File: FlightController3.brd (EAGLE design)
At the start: 50 x 85 mm, 41 parts, among them U1 NUCLEO_L432KC

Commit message: Fixed several issues
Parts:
- moved LED_SCL 0.63 mm to (17.1, 5.08)
- renumbered LED_NAV_RX to NAV_RX, LED_NAV_TX to NAV_TX
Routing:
- net !SBUS: track 70.7 -> 55.0 mm, vias 2 -> 3
- net N$5: track 0.00 -> 1.66 mm
- net N$4: track 0.00 -> 1.66 mm
- net +5V: track 186.2 -> 185.8 mm, vias 3 -> 2
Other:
- board text added: "FlightControllerBoard v.1.0"

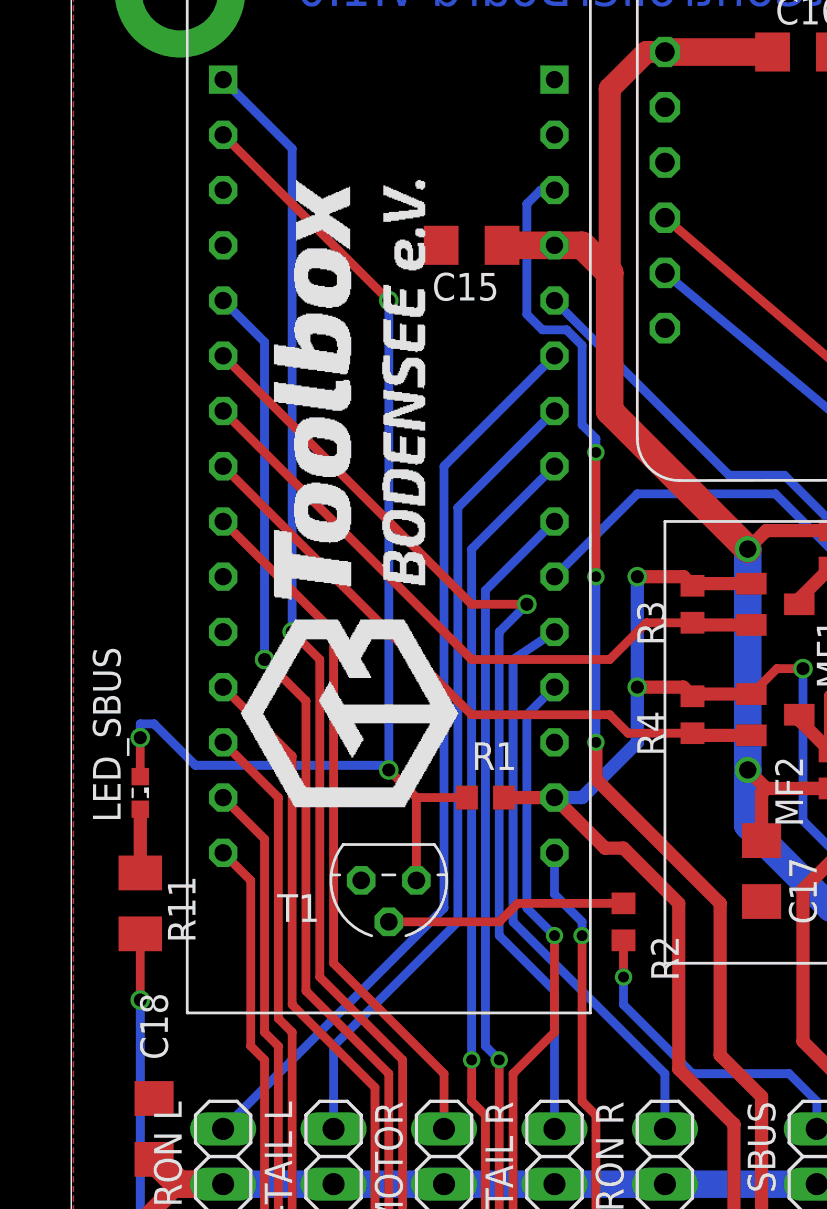
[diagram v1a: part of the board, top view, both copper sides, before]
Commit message: jumper to select between SBUS and !SBUS
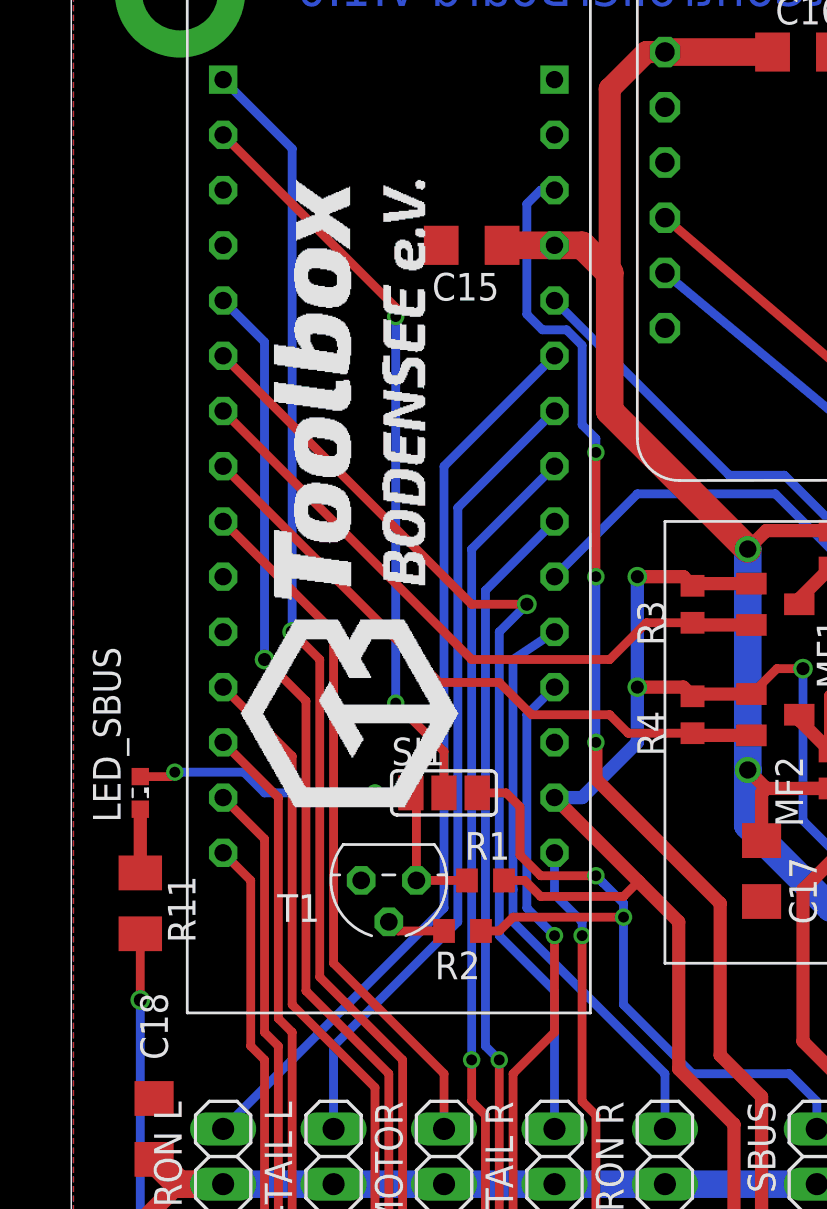
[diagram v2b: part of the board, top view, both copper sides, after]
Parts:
- added SJ1: (no value), jumper:SJ_2
- moved R2 7.42 mm to (18.0, 36.8), turned to 0 degrees
- moved R1 3.81 mm to (19.1, 39.2)
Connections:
- new net N$10: SJ1.2, U1.D0
- net !SBUS: now also SJ1.1; no longer U1.D0
- net SBUS: now also SJ1.3
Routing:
- net !SBUS: track 55.0 -> 19.4 mm, vias 3 -> 2
- net N$10: track 0.00 -> 34.5 mm, vias 0 -> 2
- net SBUS: track 15.0 -> 33.6 mm, vias 1 -> 2
- net N$1: track 11.1 -> 2.71 mm
- net +3V3: track 146.4 -> 150.4 mm

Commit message: eeprom and stuff
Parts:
- added U$3: AT24C16C, JonasLib:DIL08
- moved LED1 14.6 mm to (17.6, 3.81)
- moved R8 14.6 mm to (17.6, 7.62)
- moved LED2 14.6 mm to (21.2, 3.81)
- moved R7 14.6 mm to (21.2, 7.62)
- moved LED_SCL 4.62 mm to (12.7, 3.81)
- moved R12 4.49 mm to (10.8, 7.62)
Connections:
- net +5V: now also U$3.8
- net GND: now also U$3.4, U$3.7
- net SCL5V: now also U$3.6
- net SDA5V: now also U$3.5
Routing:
- net +5V: track 185.8 -> 177.8 mm
- net +3V3: track 150.4 -> 145.8 mm
- net SCL5V: track 116.8 -> 120.0 mm, vias 1 -> 2
- net SDA5V: track 105.1 -> 108.1 mm
- net !RST: track 87.6 -> 88.3 mm
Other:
- board text added: "P.L.A.N.E. v1.0"
- board text removed: "FlightControllerBoard v.1.0"

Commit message: various fixes
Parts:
- moved NAV_TX 0.63 mm to (42.5, 31.1)
- moved R9 0.63 mm to (42.5, 34.9)
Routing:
- net NAVBOARD_TX: track 50.1 -> 51.2 mm
- net +3V3: track 145.8 -> 145.2 mm
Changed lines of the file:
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@@
 <setting verticaltext="up"/>
 </settings>
-<grid distance="25" unitdist="mil" unit="mil" style="lines" multiple="1" display="yes" altdistance="0.025" altunitdist="inch" altunit="inch"/>
+<grid distance="25" unitdist="mil" unit="mm" style="lines" multiple="1" display="yes" altdistance="12.5" altunitdist="mil" altunit="mil"/>
 <layers>
 <layer number="1" name="Top" color="4" fill="1" visible="yes" active="yes"/>
@@
 <layer number="24" name="bOrigins" color="15" fill="1" visible="yes" active="yes"/>
 <layer number="25" name="tNames" color="7" fill="1" visible="yes" active="yes"/>
-<layer number="26" name="bNames" color="7" fill="1" visible="no" active="yes"/>
+<layer number="26" name="bNames" color="7" fill="1" visible="yes" active="yes"/>
 <layer number="27" name="tValues" color="7" fill="1" visible="no" active="yes"/>
 <layer number="28" name="bValues" color="7" fill="1" visible="no" active="yes"/>
@@
 </element>
 <element name="U$1" library="toolbox" package="TOOLBOX" value="TOOLBOX_LOGO" x="17.78" y="42.545" rot="R90"/>
-<element name="NAV_TX" library="led" library_urn="urn:adsk.eagle:library:259" package="SML0603" value="" x="43.18" y="31.115" smashed="yes" rot="R90">
-<attribute name="NAME" x="45.99" y="30.75" size="1.27" layer="25" rot="R90"/>
-<attribute name="VALUE" x="45.18" y="30.115" size="1.27" layer="27" rot="R90"/>
+<element name="NAV_TX" library="led" library_urn="urn:adsk.eagle:library:259" package="SML0603" value="" x="42.545" y="31.115" smashed="yes" rot="R90">
+<attribute name="NAME" x="45.355" y="30.75" size="1.27" layer="25" rot="R90"/>
+<attribute name="VALUE" x="44.545" y="30.115" size="1.27" layer="27" rot="R90"/>
 </element>
 <element name="NAV_RX" library="led" library_urn="urn:adsk.eagle:library:259" package="SML0603" value="" x="38.1" y="31.115" smashed="yes" rot="R90">
@@
 <attribute name="VALUE" x="40.1" y="30.115" size="1.27" layer="27" rot="R90"/>
 </element>
-<element name="R9" library="rcl" library_urn="urn:adsk.eagle:library:334" package="M1206" value="110" x="43.18" y="34.925" smashed="yes" rot="R90">
-<attribute name="NAME" x="41.91" y="33.655" size="1.27" layer="25" rot="R90"/>
-<attribute name="VALUE" x="45.72" y="33.655" size="1.27" layer="27" rot="R90"/>
+<element name="R9" library="rcl" library_urn="urn:adsk.eagle:library:334" package="M1206" value="110" x="42.545" y="34.925" smashed="yes" rot="R90">
+<attribute name="NAME" x="41.275" y="33.655" size="1.27" layer="25" rot="R90"/>
+<attribute name="VALUE" x="45.085" y="33.655" size="1.27" layer="27" rot="R90"/>
 </element>
 <element name="R10" library="rcl" library_urn="urn:adsk.eagle:library:334" package="M1206" value="110" x="38.1" y="34.925" smashed="yes" rot="R90">
@@
 <contactref element="U$3" pad="4"/>
 <contactref element="U$3" pad="7"/>
+<via x="11.43" y="30.48" extent="1-16" drill="0.35" shape="octagon"/>
+<via x="16.1925" y="29.5275" extent="1-16" drill="0.35" shape="octagon"/>
+<via x="22.5425" y="31.115" extent="1-16" drill="0.35" shape="octagon"/>
 </signal>
 <signal name="VIN">
@@
 <wire x1="22.225" y1="25.185" x2="27.305" y2="25.185" width="1.27" layer="16"/>
 <wire x1="45.085" y1="25.185" x2="46.355" y2="26.455" width="1.27" layer="16"/>
-<wire x1="46.355" y1="26.455" x2="46.355" y2="27.725" width="1.016" layer="16"/>
+<wire x1="46.355" y1="26.455" x2="46.355" y2="27.725" width="1.27" layer="16"/>
 <wire x1="23.495" y1="68.365" x2="22.225" y2="68.365" width="1.27" layer="1"/>
 <wire x1="24.765" y1="67.095" x2="23.495" y2="68.365" width="1.27" layer="1"/>
@@
 <wire x1="31.965" y1="55.245" x2="34.925" y2="55.245" width="0.6096" layer="1"/>
 <contactref element="C12" pad="1"/>
-<wire x1="46.355" y1="23.915" x2="46.355" y2="22.01" width="1.016" layer="16"/>
+<wire x1="46.355" y1="23.915" x2="46.355" y2="22.01" width="1.27" layer="16"/>
 <wire x1="46.355" y1="23.915" x2="45.085" y2="25.185" width="1.27" layer="16"/>
 <wire x1="31.965" y1="43.385" x2="31.115" y2="44.235" width="0.6096" layer="1"/>
@@
 <wire x1="4.95" y1="25.185" x2="6.985" y2="25.185" width="1.27" layer="1"/>
 <wire x1="4.95" y1="25.185" x2="3.81" y2="26.325" width="1.27" layer="1"/>
-<wire x1="2.54" y1="14.39" x2="4.445" y2="12.485" width="0.8128" layer="1"/>
-<wire x1="2.54" y1="22.775" x2="2.54" y2="14.39" width="0.8128" layer="1"/>
-<wire x1="2.54" y1="22.775" x2="4.95" y2="25.185" width="0.8128" layer="1"/>
+<wire x1="2.54" y1="14.39" x2="4.445" y2="12.485" width="1.27" layer="1"/>
+<wire x1="2.54" y1="22.775" x2="2.54" y2="14.39" width="1.27" layer="1"/>
+<wire x1="2.54" y1="22.775" x2="4.95" y2="25.185" width="1.27" layer="1"/>
 <wire x1="33.515" y1="43.385" x2="34.925" y2="43.385" width="0.6096" layer="1"/>
 <wire x1="35.14" y1="38.1" x2="34.925" y2="37.885" width="0.6096" layer="16"/>
-<wire x1="27.305" y1="77.255" x2="26.455" y2="77.255" width="1.016" layer="1"/>
-<wire x1="24.765" y1="75.565" x2="24.765" y2="67.095" width="1.016" layer="1"/>
-<wire x1="26.455" y1="77.255" x2="24.765" y2="75.565" width="1.016" layer="1"/>
+<wire x1="27.305" y1="77.255" x2="26.455" y2="77.255" width="1.27" layer="1"/>
+<wire x1="24.765" y1="75.565" x2="24.765" y2="67.095" width="1.27" layer="1"/>
+<wire x1="26.455" y1="77.255" x2="24.765" y2="75.565" width="1.27" layer="1"/>
 <contactref element="R12" pad="2"/>
 <wire x1="31.75" y1="40.985" x2="31.75" y2="43.17" width="0.6096" layer="1"/>
@@
 <contactref element="U1" pad="A5"/>
 <wire x1="22.225" y1="60.745" x2="17.78" y2="56.3" width="0.4064" layer="16"/>
-<wire x1="17.78" y1="56.3" x2="17.78" y2="37.25" width="0.4064" layer="16"/>
-<wire x1="17.78" y1="37.25" x2="12.065" y2="31.535" width="0.4064" layer="16"/>
-<wire x1="12.065" y1="31.535" x2="12.065" y2="27.725" width="0.4064" layer="16"/>
+<wire x1="17.78" y1="34.925" x2="12.065" y2="29.21" width="0.4064" layer="16"/>
+<wire x1="12.065" y1="29.21" x2="12.065" y2="27.725" width="0.4064" layer="16"/>
+<wire x1="17.78" y1="56.3" x2="17.78" y2="34.925" width="0.4064" layer="16"/>
 </signal>
 <signal name="PPM_V_TAIL_R">
@@
 <wire x1="18.415" y1="51.855" x2="20.955" y2="51.855" width="0.4064" layer="1"/>
 <wire x1="20.955" y1="51.855" x2="19.685" y2="50.585" width="0.4064" layer="16"/>
-<wire x1="19.685" y1="36.615" x2="22.225" y2="34.075" width="0.4064" layer="16"/>
-<wire x1="22.225" y1="34.075" x2="22.225" y2="27.725" width="0.4064" layer="16"/>
-<wire x1="19.685" y1="50.585" x2="19.685" y2="36.615" width="0.4064" layer="16"/>
+<wire x1="19.685" y1="32.385" x2="22.225" y2="29.845" width="0.4064" layer="16"/>
+<wire x1="22.225" y1="29.845" x2="22.225" y2="27.725" width="0.4064" layer="16"/>
+<wire x1="19.685" y1="50.585" x2="19.685" y2="32.385" width="0.4064" layer="16"/>
 </signal>
 <signal name="SBUS">
@@
 <wire x1="5.5626" y1="15.48793125" x2="5.5626" y2="13.9074" width="0.4064" layer="16"/>
 <wire x1="3.27053125" y1="17.78" x2="5.5626" y2="15.48793125" width="0.4064" layer="16"/>
-<wire x1="43.18" y1="36.325" x2="43.18" y2="40.005" width="0.4064" layer="1"/>
-<wire x1="38.1" y1="36.325" x2="38.1" y2="40.005" width="0.4064" layer="1"/>
+<wire x1="38.1" y1="40.005" x2="38.1" y2="36.325" width="0.4064" layer="1"/>
 <via x="38.1" y="40.005" extent="1-16" drill="0.6" shape="octagon"/>
-<via x="43.18" y="40.005" extent="1-16" drill="0.6" shape="octagon"/>
-<wire x1="43.18" y1="40.005" x2="38.1" y2="40.005" width="0.4064" layer="16"/>
+<wire x1="42.545" y1="40.005" x2="38.1" y2="40.005" width="0.4064" layer="16"/>
 <wire x1="38.1" y1="40.005" x2="35.56" y2="40.005" width="0.4064" layer="16"/>
 <wire x1="35.56" y1="40.005" x2="33.655" y2="41.91" width="0.4064" layer="16"/>
@@
 <wire x1="8.255" y1="11.215" x2="23.71" y2="11.215" width="0.6096" layer="1"/>
 <wire x1="23.71" y1="11.215" x2="24.13" y2="10.795" width="0.6096" layer="1"/>
+<wire x1="42.545" y1="36.325" x2="42.545" y2="40.005" width="0.4064" layer="1"/>
+<via x="42.545" y="40.005" extent="1-16" drill="0.6" shape="octagon"/>
 </signal>
 <signal name="NAVBOARD_TX">
@@
 <contactref element="U1" pad="A7"/>
 <via x="41.275" y="46.775" extent="1-16" drill="0.6" shape="octagon"/>
-<wire x1="41.275" y1="28.575" x2="41.275" y2="27.725" width="0.4064" layer="1"/>
-<wire x1="41.275" y1="28.575" x2="41.275" y2="46.775" width="0.4064" layer="1"/>
 <wire x1="41.275" y1="46.775" x2="41.275" y2="49.315" width="0.4064" layer="16"/>
 <wire x1="32.7992" y1="57.7908" x2="41.275" y2="49.315" width="0.4064" layer="16"/>
@@
 <wire x1="30.2592" y1="57.7908" x2="32.7992" y2="57.7908" width="0.4064" layer="16"/>
 <contactref element="NAV_TX" pad="C"/>
-<wire x1="43.18" y1="30.365" x2="41.39" y2="28.575" width="0.4064" layer="1"/>
-<wire x1="41.39" y1="28.575" x2="41.275" y2="28.575" width="0.4064" layer="1"/>
+<wire x1="41.275" y1="29.095" x2="42.545" y2="30.365" width="0.4064" layer="1"/>
+<wire x1="41.275" y1="29.095" x2="41.275" y2="27.725" width="0.4064" layer="1"/>
+<wire x1="41.275" y1="27.725" x2="41.275" y2="29.21" width="0.4064" layer="1"/>
+<wire x1="41.275" y1="29.21" x2="40.64" y2="29.845" width="0.4064" layer="1"/>
+<wire x1="40.64" y1="29.845" x2="40.64" y2="44.45" width="0.4064" layer="1"/>
+<wire x1="40.64" y1="44.45" x2="41.275" y2="45.085" width="0.4064" layer="1"/>
+<wire x1="41.275" y1="45.085" x2="41.275" y2="46.775" width="0.4064" layer="1"/>
 </signal>
 <signal name="NAVBOARD_RX">
@@
 <contactref element="NAV_TX" pad="A"/>
 <contactref element="R9" pad="1"/>
-<wire x1="43.18" y1="33.525" x2="43.18" y2="31.865" width="0.4064" layer="1"/>
+<wire x1="42.545" y1="33.525" x2="42.545" y2="31.865" width="0.4064" layer="1"/>
 </signal>
 <signal name="N$5">
